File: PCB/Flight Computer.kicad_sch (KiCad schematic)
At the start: 0 parts

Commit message: Made changes discussed in the design review
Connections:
- no-connect marks 16 -> 20
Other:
- sheet MCU ports: added PB10, PC12; removed PA8, PC9

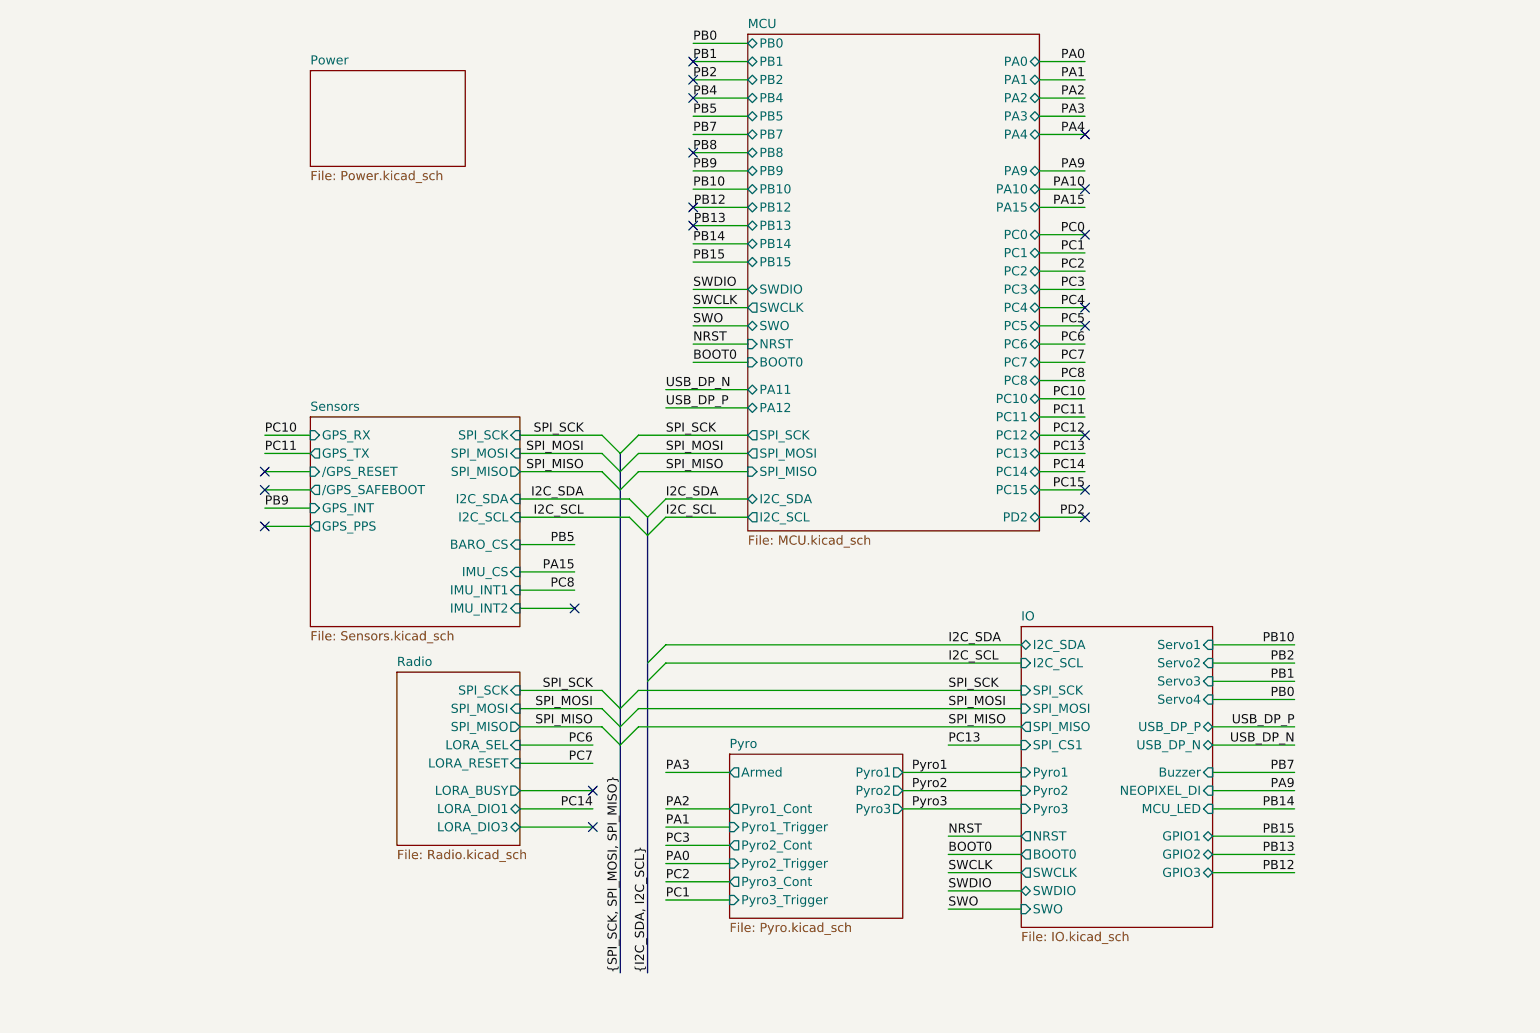
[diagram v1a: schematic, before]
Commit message: Added an image of the pin mapping from cubemx to the schematic
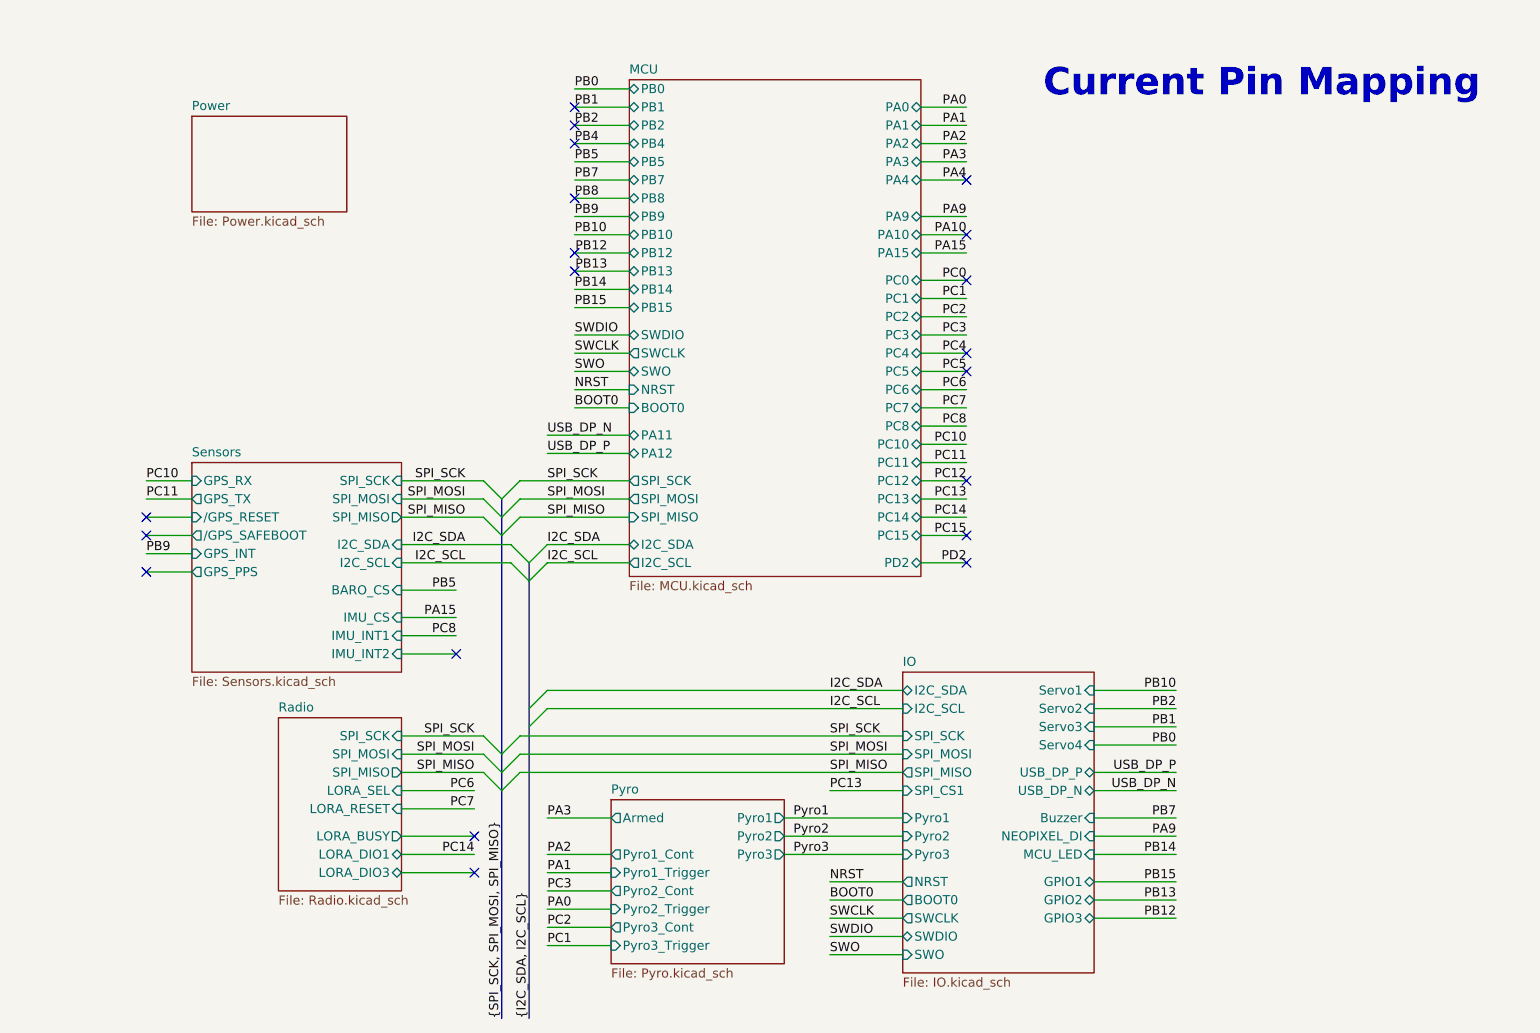
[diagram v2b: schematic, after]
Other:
- note added: "Current Pin Mapping"

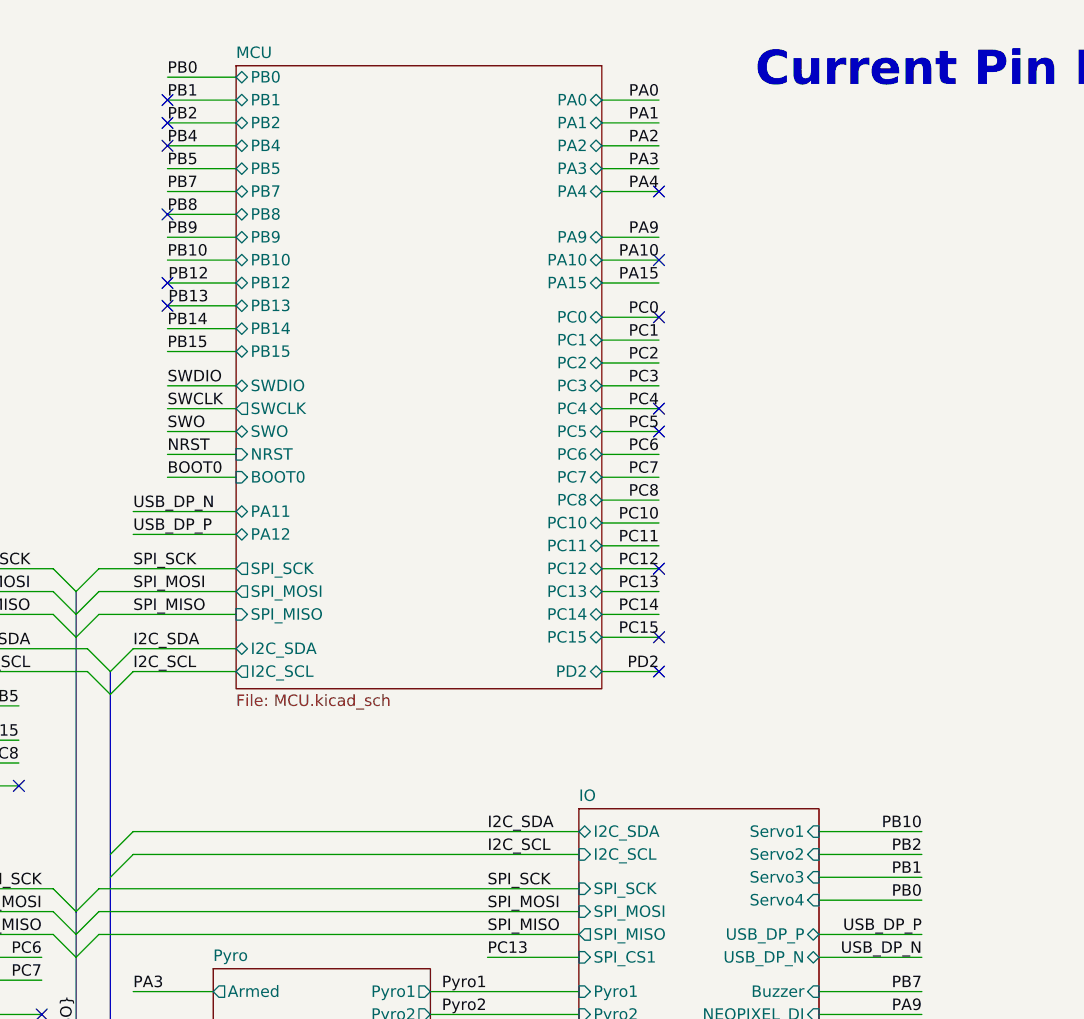
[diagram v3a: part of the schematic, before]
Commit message: - Swapped MCU for the STM32F405 series cause the F446 is out of stock for the foreseeable future
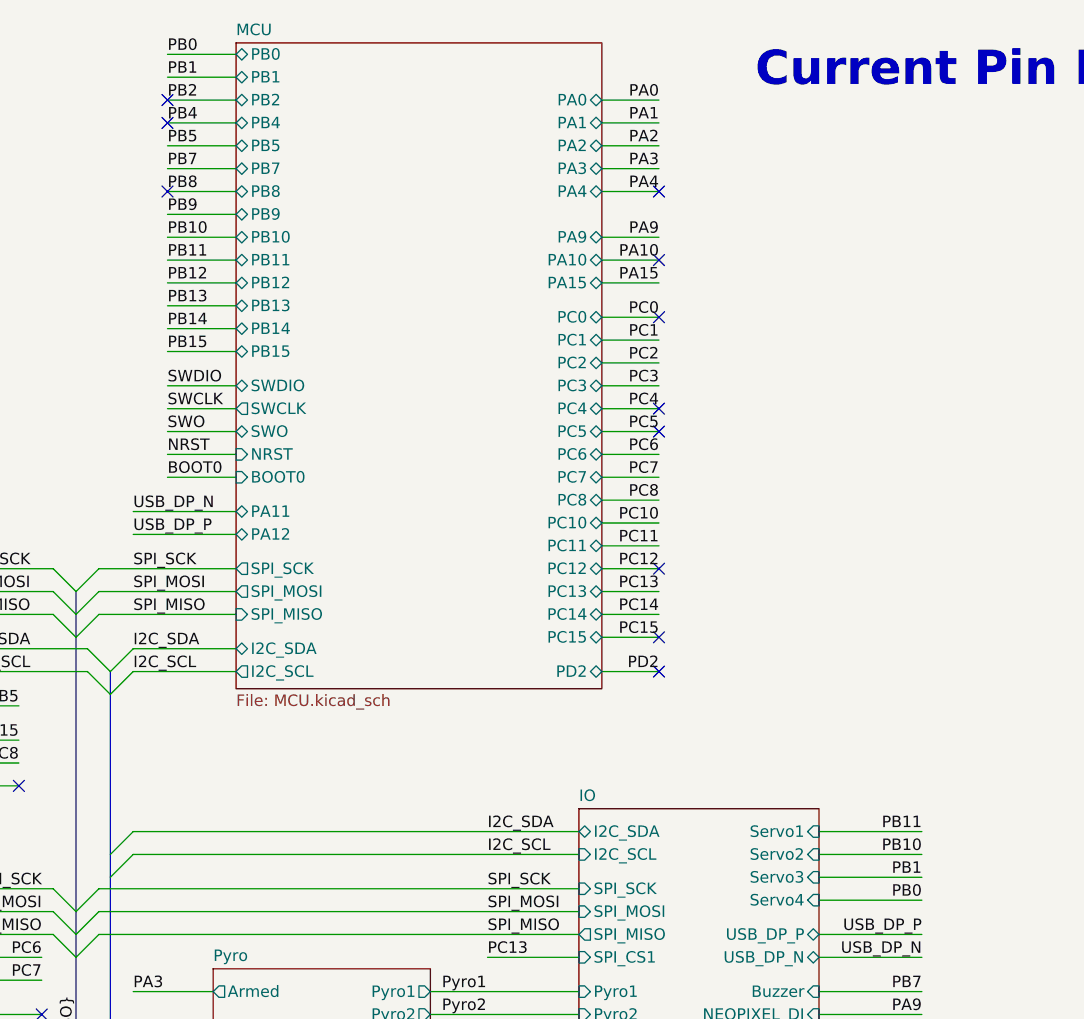
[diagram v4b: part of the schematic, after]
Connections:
- no-connect marks 20 -> 17
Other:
- sheet MCU ports: added PB11; removed none
